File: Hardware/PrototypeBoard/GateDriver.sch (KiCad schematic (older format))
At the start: 38 parts, among them U4 TLE7185-1E

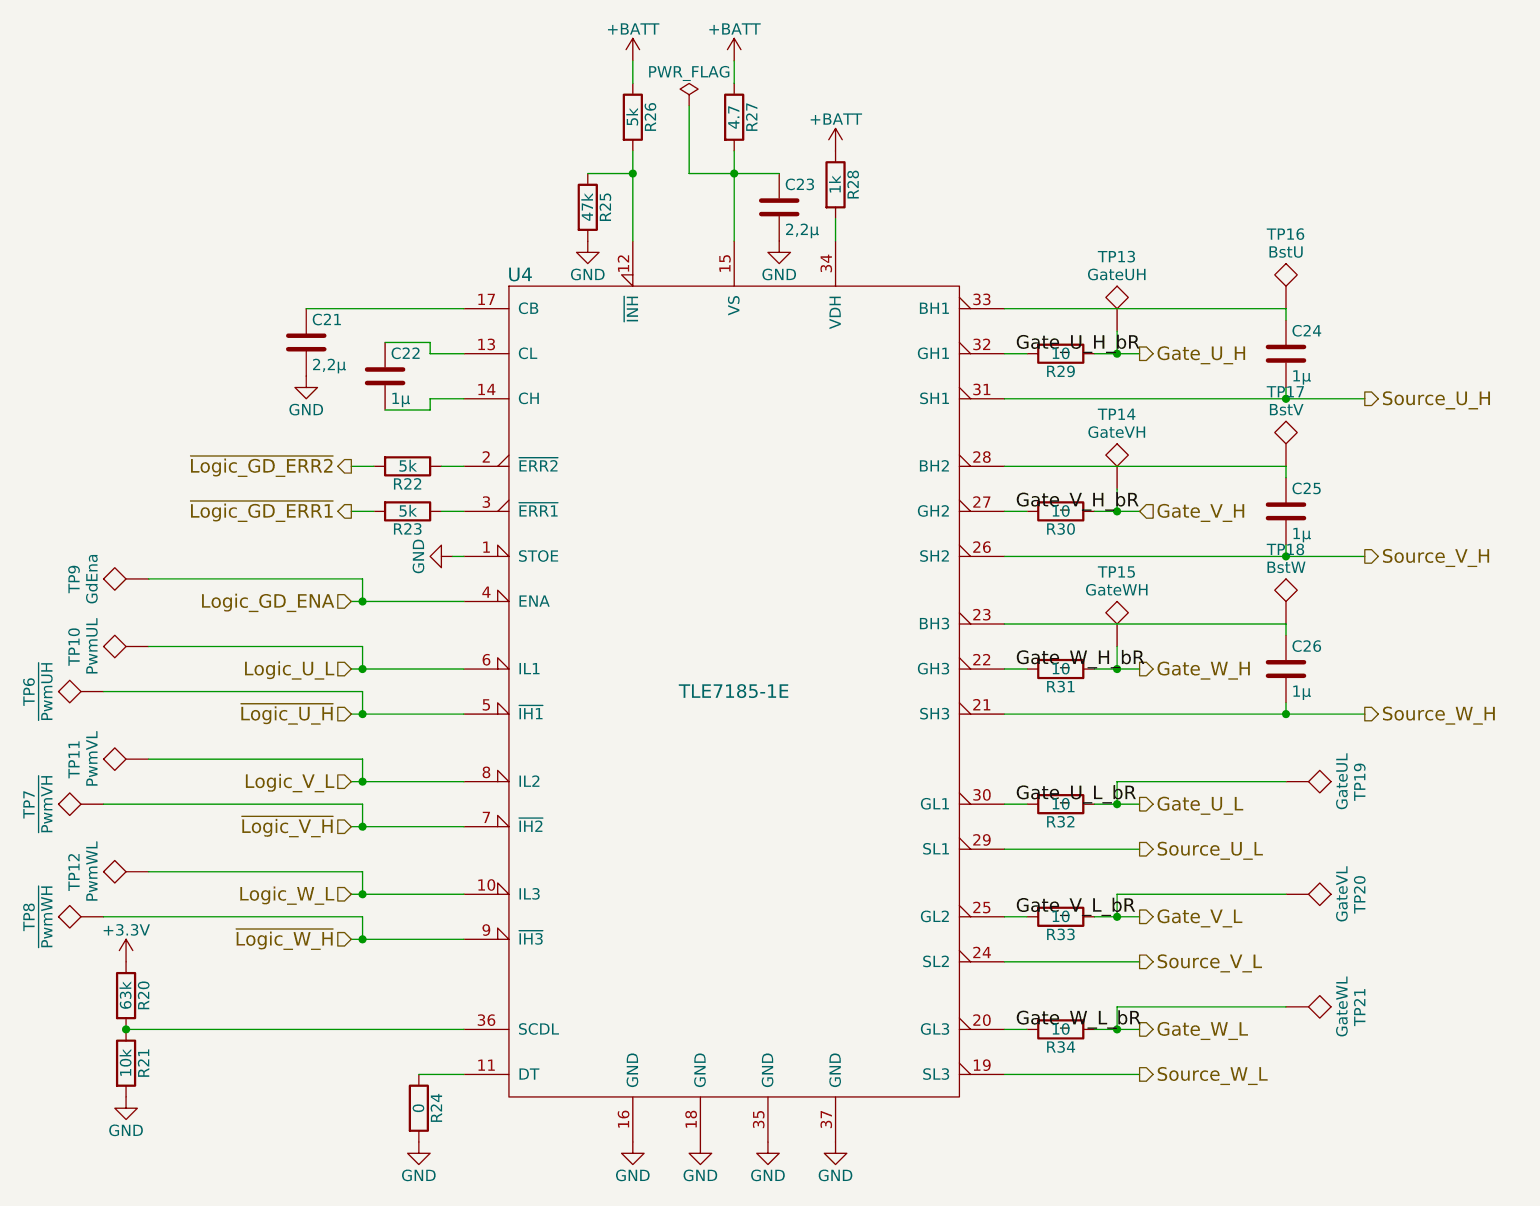
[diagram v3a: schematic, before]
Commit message: Some deduplication, renaming and cleanups in the schematic
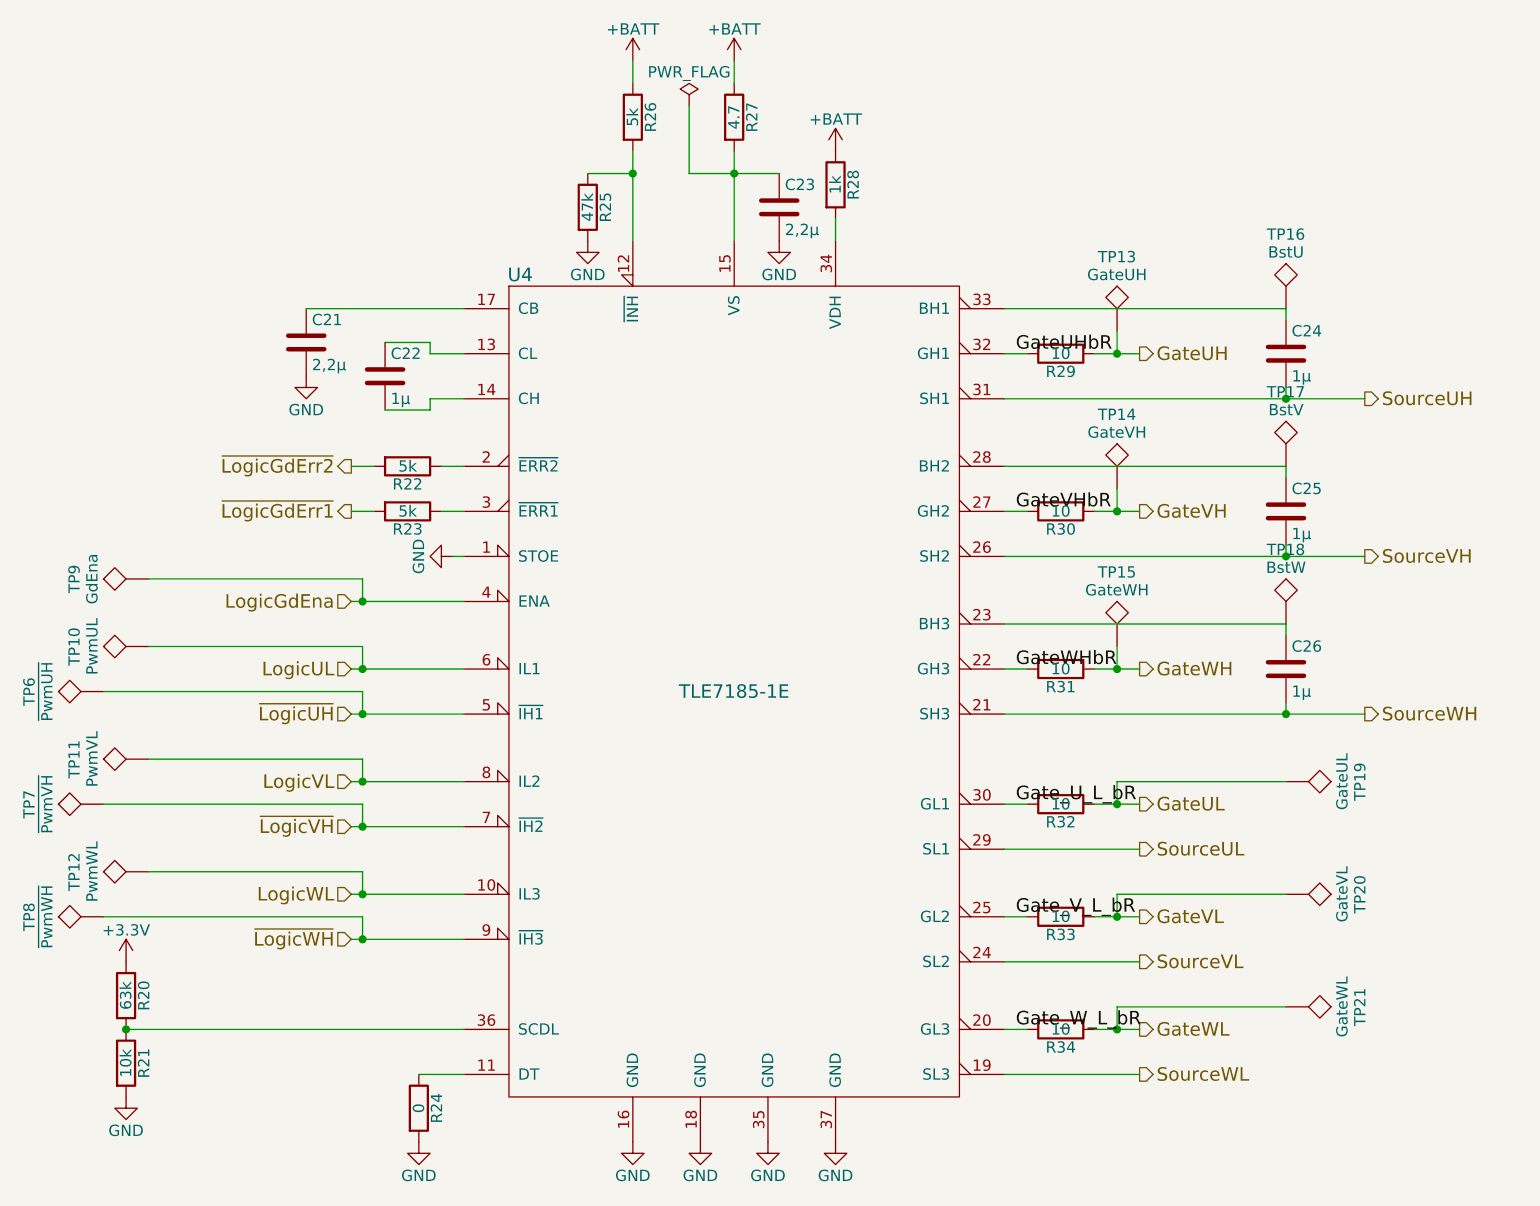
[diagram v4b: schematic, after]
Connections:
- net Gate_U_H renamed GateUH
- net Gate_U_H_bR renamed GateUHbR
- net Gate_U_L renamed GateUL
- net Gate_V_H renamed GateVH
- net Gate_V_H_bR renamed GateVHbR
- net Gate_V_L renamed GateVL
- net Gate_W_H renamed GateWH
- net Gate_W_H_bR renamed GateWHbR
- net Gate_W_L renamed GateWL
- net Logic_GD_ENA renamed LogicGdEna
- net Logic_U_L renamed LogicUL
- net Logic_V_L renamed LogicVL
- net Logic_W_L renamed LogicWL
- net Source_U_H renamed SourceUH
- net Source_U_L renamed SourceUL
- net Source_V_H renamed SourceVH
- net Source_V_L renamed SourceVL
- net Source_W_H renamed SourceWH
- net Source_W_L renamed SourceWL
- net ~Logic_GD_ERR1 renamed ~LogicGdErr1
- net ~Logic_GD_ERR2 renamed ~LogicGdErr2
- net ~Logic_U_H renamed ~LogicUH
- net ~Logic_V_H renamed ~LogicVH
- net ~Logic_W_H renamed ~LogicWH
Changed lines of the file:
@@
 $Descr A4 11693 8268
 encoding utf-8
-Sheet 5 8
+Sheet 5 13
 Title ""
 Date ""
@@
 $EndComp
 Text HLabel 2800 3500 0    60   Input ~ 0
-Logic_U_L
+LogicUL
 Text HLabel 2800 3700 0    60   Input ~ 0
-~Logic_U_H
+~LogicUH
 Text HLabel 2800 4000 0    60   Input ~ 0
-Logic_V_L
+LogicVL
 Text HLabel 2800 4200 0    60   Input ~ 0
-~Logic_V_H
+~LogicVH
 Text HLabel 2800 4500 0    60   Input ~ 0
-Logic_W_L
+LogicWL
 Text HLabel 2800 4700 0    60   Input ~ 0
-~Logic_W_H
+~LogicWH
 Text HLabel 2800 3200 0    60   Input ~ 0
-Logic_GD_ENA
+LogicGdEna
 $Comp
 L Device:R R23
@@
 	3300 2800 3200 2800
 Text HLabel 2800 2800 0    60   Output ~ 0
-~Logic_GD_ERR1
+~LogicGdErr1
 Text HLabel 2800 2600 0    60   Output ~ 0
-~Logic_GD_ERR2
+~LogicGdErr2
 $Comp
 L Device:C C22
@@
 $EndComp
 Text HLabel 7300 2300 2    60   Output ~ 0
-Source_U_H
+SourceUH
 Text HLabel 7300 3000 2    60   Output ~ 0
-Source_V_H
+SourceVH
 Text HLabel 7300 3700 2    60   Output ~ 0
-Source_W_H
+SourceWH
 $Comp
 L Device:C C24
@@
 	6950 3300 6950 3350
 Text HLabel 6300 4300 2    60   Output ~ 0
-Source_U_L
+SourceUL
 Text HLabel 6300 4800 2    60   Output ~ 0
-Source_V_L
+SourceVL
 Text HLabel 6300 5300 2    60   Output ~ 0
-Source_W_L
+SourceWL
 Text HLabel 6300 5100 2    60   Output ~ 0
-Gate_W_L
+GateWL
 $Comp
 L Device:R R34
@@
 $EndComp
 Text HLabel 6300 4600 2    60   Output ~ 0
-Gate_V_L
+GateVL
 Text HLabel 6300 4100 2    60   Output ~ 0
-Gate_U_L
+GateUL
 $Comp
 L Device:R R32
@@
 	3850 1300 4050 1300
 Text HLabel 6300 3500 2    60   Output ~ 0
-Gate_W_H
-Text HLabel 6300 2800 2    60   Input ~ 0
-Gate_V_H
+GateWH
+Text HLabel 6300 2800 2    60   Output ~ 0
+GateVH
 Text HLabel 6300 2100 2    60   Output ~ 0
-Gate_U_H
+GateUH
 $Comp
 L power:GND #PWR046
@@
 	4300 1000 4300 1300
 Text Label 5750 2100 0    60   ~ 0
-Gate_U_H_bR
+GateUHbR
 Text Label 5750 2800 0    60   ~ 0
-Gate_V_H_bR
+GateVHbR
 Text Label 5750 3500 0    60   ~ 0
-Gate_W_H_bR
+GateWHbR
 Text Label 5750 4100 0    60   ~ 0
 Gate_U_L_bR
